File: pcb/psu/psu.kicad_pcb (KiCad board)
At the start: 2 copper layers, 44.4 x 30.5 mm, 4 parts, among them J1 VIN, J2 HEADER-1x04, J3 HEADER-1x01

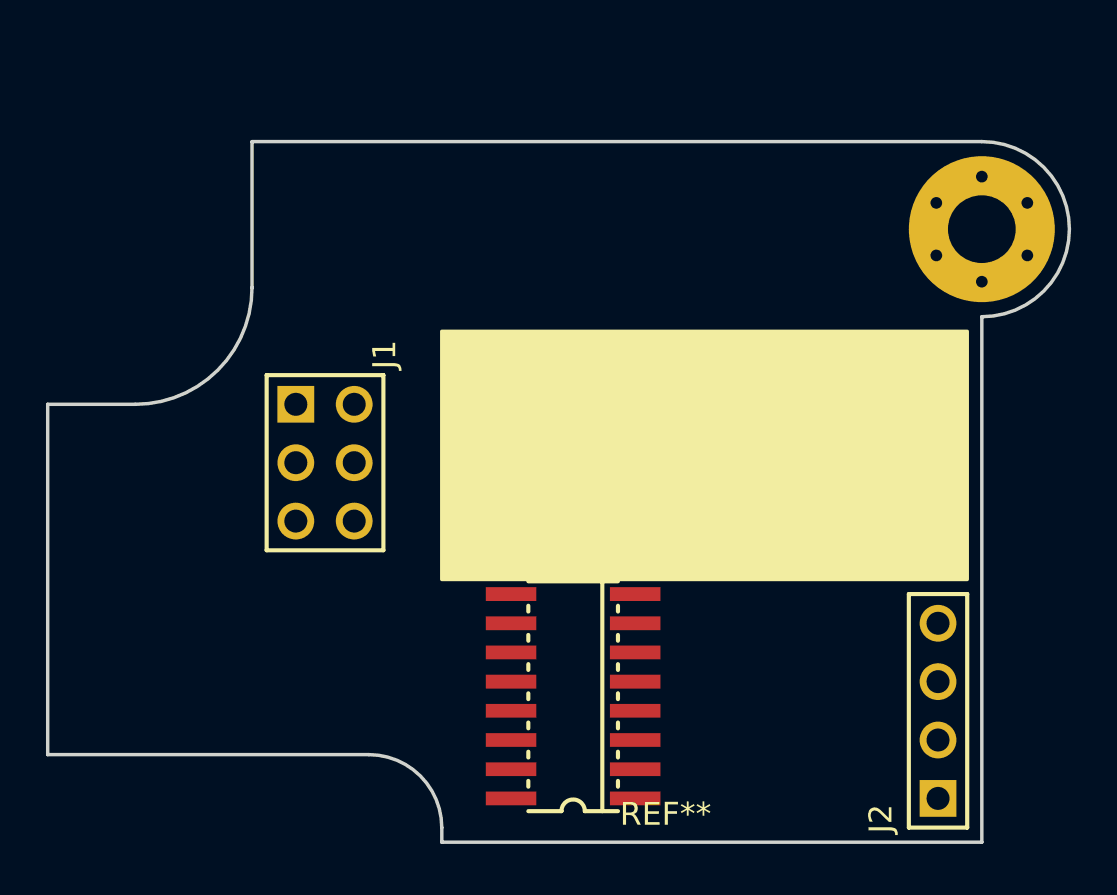
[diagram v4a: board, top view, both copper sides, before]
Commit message: PSU board schematics/layout
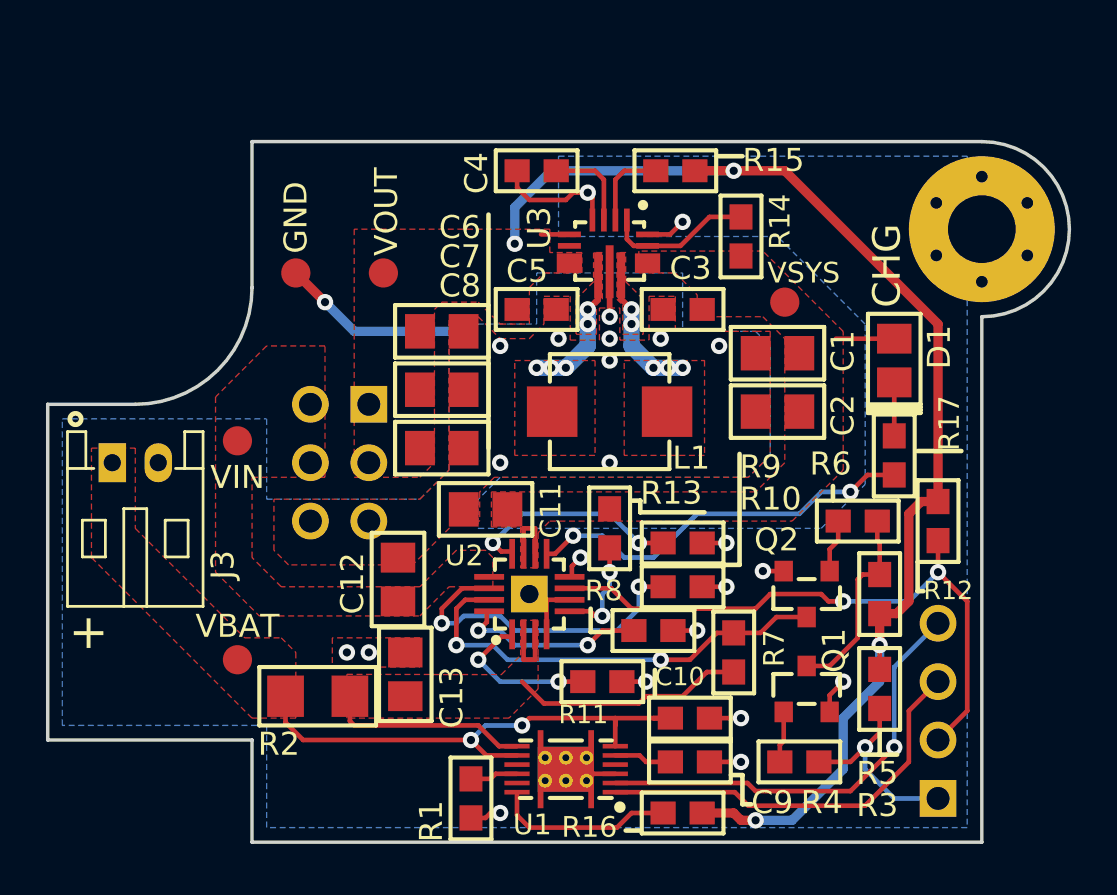
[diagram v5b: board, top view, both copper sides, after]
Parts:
- removed the REF** at (155.6, 114.3)
- added C1: 10uF, smt:C-0805, F.Cu at (164.5, 99.4)
- added C10: 1uF, smt:C-0603, F.Cu at (160.7, 115.3)
- added C11: 10uF, smt:C-0805, F.Cu at (151.8, 106.2)
- added C12: 10uF, smt:C-0805, F.Cu at (148.0, 109.2)
- added C13: 10uF, smt:C-0805, F.Cu at (148.3, 113.3)
- added C2: 10uF, smt:C-0805, F.Cu at (164.5, 101.9)
- added C3: 10uF, smt:C-0603, F.Cu at (160.3, 97.5)
- added C4: 100nF, smt:C-0603, F.Cu at (154.0, 91.4)
- added C5: 10uF, smt:C-0603, F.Cu at (154.0, 97.5)
- added C6: 22uF, smt:C-0805, F.Cu at (149.9, 98.4)
- added C7: 22uF, smt:C-0805, F.Cu at (149.9, 101.0)
- added C8: 22uF, smt:C-0805, F.Cu at (149.9, 103.5)
- added C9: 470nF, smt:C-0603, F.Cu at (160.7, 117.2)
- added D1: LED, smt:LED-0805, F.Cu at (169.5, 99.7)
- added H1: Hole, conn-wire-pads:Hole-Screw-#4, F.Cu at (173.4, 94.0)
- added L1: 1.5uH, smt-inductor:SPM5030-HZ, F.Cu at (157.2, 101.9)
- added Q1: MMST3904, smt-sot:SOT23, F.Cu at (165.7, 114.0)
- added Q2: MMST3904, smt-sot:SOT23, F.Cu at (165.7, 109.9)
- added R1: 10k, smt:R-0603, F.Cu at (151.1, 118.7)
- added R10: 0, smt:R-0603, F.Cu at (160.3, 109.5)
- added R11: 10k, smt:R-0603, F.Cu at (156.8, 113.7)
- added R12: 100k, smt:R-0603, F.Cu at (171.4, 106.7)
- added R13: 10k, smt:R-0603, F.Cu at (157.2, 107.0)
- added R14: 10k, smt:R-0603, F.Cu at (162.9, 94.3)
- added R15: 10k, smt:R-0603, F.Cu at (160.0, 91.4)
- added R16: 10k, smt:R-0603, F.Cu at (160.3, 119.4)
- added R17: 680, smt:R-0603, F.Cu at (169.5, 103.8)
- added R2: 0.01 1%, smt:R-1206, F.Cu at (144.5, 114.3)
- added R3: 100k, smt:R-0603, F.Cu at (168.9, 114.0)
- added R4: 100k, smt:R-0603, F.Cu at (165.4, 117.2)
- added R5: 100k, smt:R-0603, F.Cu at (168.9, 109.9)
- added R6: 100k, smt:R-0603, F.Cu at (168.0, 106.7)
- added R7: 787k, smt:R-0603, F.Cu at (162.6, 112.4)
- added R8: 5.6k, smt:R-0603, F.Cu at (159.1, 111.4)
- added R9: 1.1k, smt:R-0603, F.Cu at (160.3, 107.6)
- added REF**: VAL**, symbols:LOGO-OSHW-150, B.Cu at (137.8, 110.5)
- added REF**: VAL**, symbols:SIGNATURE_SILK, B.Cu at (143.5, 114.6)
- added TP1: VBAT, conn-wire-pads:TEST-POINT-50, F.Cu at (141.0, 112.7)
- added TP2: VIN, conn-wire-pads:TEST-POINT-50, F.Cu at (141.0, 103.2)
- added TP3: VSYS, conn-wire-pads:TEST-POINT-50, F.Cu at (164.8, 97.2)
- added TP4: GND, conn-wire-pads:TEST-POINT-50, F.Cu at (143.5, 95.9)
- added TP5: VOUT, conn-wire-pads:TEST-POINT-50, F.Cu at (147.3, 95.9)
- added U1: BQ27441-G1, smt-son:PDSO-N12, F.Cu at (155.3, 117.5)
- added U2: BQ24075, smt-qfn:QFN16-EP-3x3, F.Cu at (153.7, 109.9)
- added U3: TPS630701, smt-qfn:VQFN15N, F.Cu at (157.2, 94.9)
- J1: moved to B.Cu
- J2: value HEADER-1x04 -> SIGNAL; moved to B.Cu
- J3: value HEADER-1x01 -> BATTERY; footprint conn-wire-pads:Hole-Screw-#4 -> conn-jst:S2B-PH-K
- moved J3 38.2 mm to (136.5, 104.1)
- moved J1 0.63 mm to (145.4, 104.1)
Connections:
- J1 pad 1: Net-(J1-Pad1) -> +5V
- J1 pad 2: Net-(J1-Pad2) -> +VIN
- J1 pad 4: +5V -> +VIN
- J2 pad 1: Net-(J2-Pad1) -> /SYSOFF
- J2 pad 2: Net-(J2-Pad2) -> /ON_BATT
- J2 pad 3: Net-(J2-Pad3) -> /SDA
- J2 pad 4: Net-(J2-Pad4) -> /SCL
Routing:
- net +5V: track 0.00 -> 56.5 mm, vias 0 -> 4
- net GND: track 0.00 -> 33.4 mm, vias 0 -> 24
- net /ON_BATT: track 0.00 -> 26.9 mm, vias 0 -> 2
- net /BATT_IN: track 0.00 -> 22.8 mm, vias 0 -> 2
- net +BATT: track 0.00 -> 21.7 mm
- net Net-(Q2-Pad3): track 0.00 -> 19.3 mm, vias 0 -> 2
- net /SCL: track 0.00 -> 19.3 mm, vias 0 -> 1
- net /SDA: track 0.00 -> 18.5 mm
- net /~CHG: track 0.00 -> 17.3 mm, vias 0 -> 2
- net Net-(R10-Pad2): track 0.00 -> 14.3 mm, vias 0 -> 2
- net Net-(R9-Pad2): track 0.00 -> 9.45 mm, vias 0 -> 2
- net /SYSOFF: track 0.00 -> 8.88 mm, vias 0 -> 1
- net Net-(Q1-Pad3): track 0.00 -> 8.68 mm
- net Net-(R8-Pad2): track 0.00 -> 8.29 mm, vias 0 -> 2
- net Net-(R16-Pad1): track 0.00 -> 7.84 mm
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- added copper zone on F.Cu, net +5V
- added copper zone on F.Cu, net +BATT
- added copper zone on F.Cu, net +SYS
- added copper zone on F.Cu, net +VIN
- added copper zone on F.Cu, net /BATT_IN
- added copper zone on F.Cu, net /L1
- added copper zone on F.Cu, net /L2
- added copper zone on B.Cu, net GND
- added copper zone on F.Cu, net GND
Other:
- outline, holes or cut-outs redrawn
- net class Default: clearance 0.2 -> 0.1778; trace_width 0.25 -> 0.2032; via_dia 0.8 -> 0.7112; via_drill 0.4 -> 0.3556
- rule pad_to_mask_clearance: 0.2 -> 0.05
- rule trace_clearance: 0.2 -> 0.1778
- rule trace_min: 0.2 -> 0.2032
- rule via_min_size: 0.4 -> 0.4064
- board text added: "+"
- board text added: "11/18"
- board text added: "AV3-PC-07"
- board text added: "CHG"
- board text added: "REV. A"
